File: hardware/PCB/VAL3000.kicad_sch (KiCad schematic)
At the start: 60 parts, among them J1 1984617, J3 B4B-XH-A, J4 B4B-XH-A, J5 OSTVN02A150, J6 OSTVN02A150, J7 Conn_01x02_Pin, SW7 TS-1088-AR02016, SW8 TS-1088-AR02016, U1 RT9080-33GJ5, U2 TMC2209-LA-T, U3 TC-6615-4.5-160G, U4 TC-6615-4.5-160G, U5 TC-6615-4.5-160G, U6 ESP32-C3-WROOM-02, U9 AP63203QWU-7

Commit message: PCB
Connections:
- net GND: now also J5.2; no longer J5.1
- net USER_4/END_2: now also J5.1; no longer J5.2
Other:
- moved on the sheet: J5
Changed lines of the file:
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@@
 	(wire
 		(pts
-			(xy 328.93 151.13) (xy 328.93 157.48)
+			(xy 328.93 149.86) (xy 328.93 157.48)
 		)
 		(stroke
@@
 	(wire
 		(pts
-			(xy 321.31 148.59) (xy 328.93 148.59)
+			(xy 321.31 147.32) (xy 328.93 147.32)
 		)
 		(stroke
@@
 	(wire
 		(pts
-			(xy 321.31 151.13) (xy 328.93 151.13)
+			(xy 321.31 149.86) (xy 328.93 149.86)
 		)
 		(stroke
@@
 	(global_label "USER_4{slash}END_2"
 		(shape input)
-		(at 328.93 148.59 0)
+		(at 328.93 147.32 0)
 		(fields_autoplaced yes)
 		(effects
@@
 		)
 		(property "Intersheetrefs" "${INTERSHEET_REFS}"
-			(at 346.3084 148.59 0)
+			(at 346.3084 147.32 0)
 			(effects
 				(font
@@
 	(symbol
 		(lib_id "2025-11-27_21-36-42:OSTVN02A150")
-		(at 321.31 151.13 180)
+		(at 321.31 147.32 0)
+		(mirror y)
 		(unit 1)
 		(exclude_from_sim no)
@@
 		(on_board yes)
 		(dnp no)
-		(fields_autoplaced yes)
 		(property "Reference" "J5"
-			(at 312.42 140.97 0)
+			(at 312.42 157.48 0)
 			(effects
 				(font
@@
 		)
 		(property "Value" "OSTVN02A150"
-			(at 312.42 143.51 0)
+			(at 312.42 154.94 0)
 			(effects
 				(font
@@
 		)
 		(property "Footprint" "footprints:CONN_OSTVN02A150_OST"
-			(at 321.31 151.13 0)
+			(at 321.31 147.32 0)
 			(effects
 				(font
@@
 		)
 		(property "Datasheet" "OSTVN02A150"
-			(at 321.31 151.13 0)
+			(at 321.31 147.32 0)
 			(effects
 				(font
@@
 		)
 		(property "Description" ""
-			(at 321.31 151.13 0)
+			(at 321.31 147.32 0)
 			(effects
 				(font

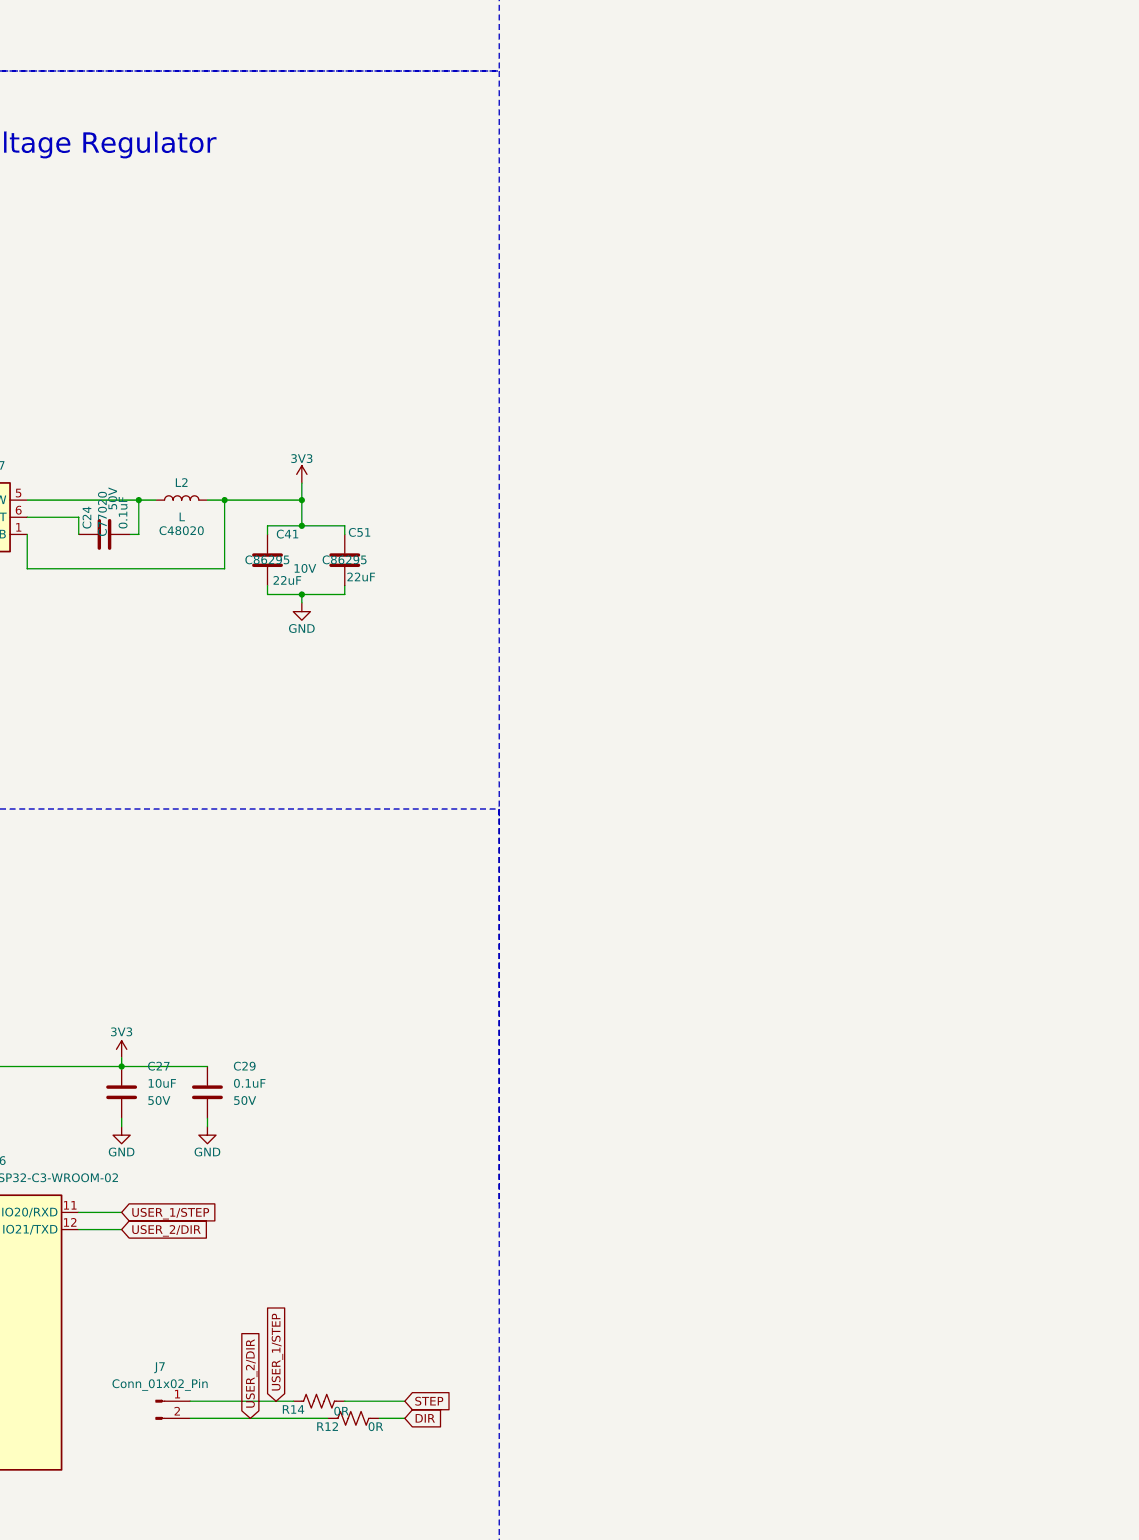
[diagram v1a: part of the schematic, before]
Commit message: Button fixes and PCB NEMA 17 holes
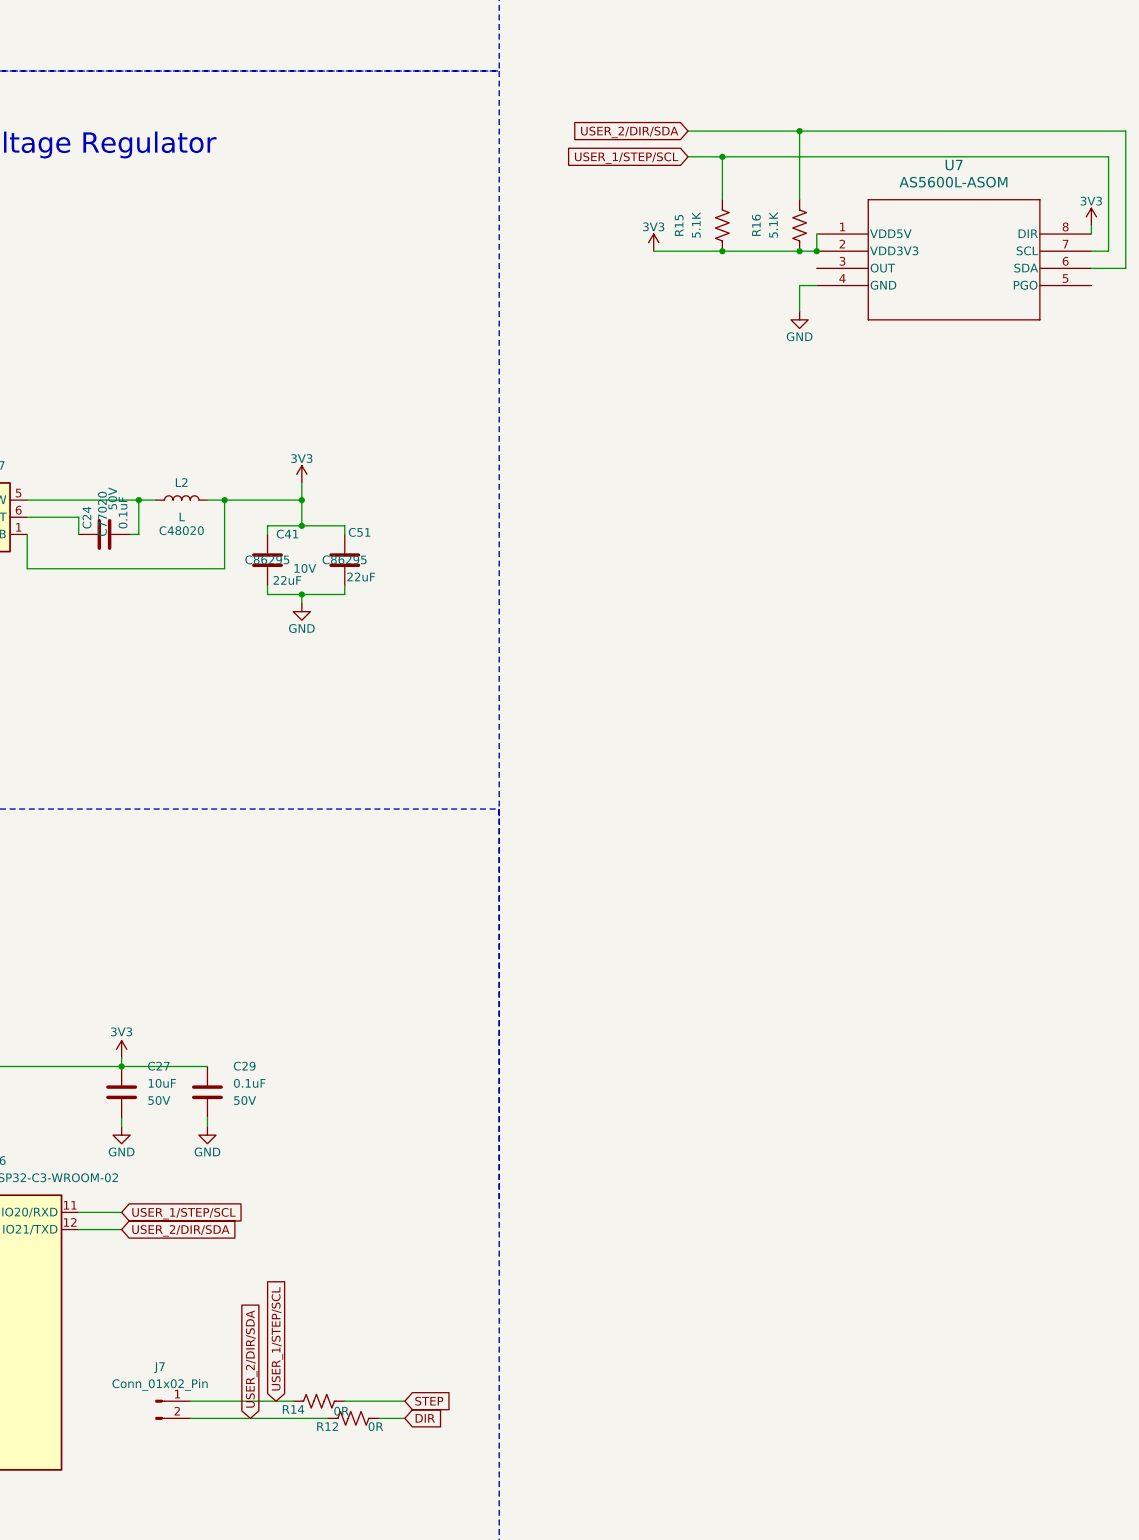
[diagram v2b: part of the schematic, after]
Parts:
- added R15, R16: 5.1K, Resistor_SMD:R_0402_1005Metric, symbol SparkFun-Resistor:10k_0402
- added U7: AS5600L-ASOM, AS5600L-ASOM_AMS:AS5600L-ASOM_AMS, symbol 2025-11-30_16-50-14:AS5600L-ASOM
- J5, J6: now left out of the parts list
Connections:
- net 3V3: now also R15.1, R16.1, U7.1 (VDD5V), U7.2 (VDD3V3), U7.8 (DIR)
- net GND: now also U7.4 (GND)
- net USER_1/STEP renamed USER_1/STEP/SCL
- net USER_1/STEP/SCL: now also R15.2, U7.7 (SCL)
- net USER_2/DIR renamed USER_2/DIR/SDA
- net USER_2/DIR/SDA: now also R16.2, U7.6 (SDA)
